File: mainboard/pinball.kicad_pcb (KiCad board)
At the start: 2 copper layers, 35 parts, among them CON1 AVR-ISP-6, IC1 ATMEGA328-A, P1 SCREW_PLACEHOLDER, P2 SCREW_PLACEHOLDER, P3 SCREW_PLACEHOLDER, P4 SCREW_PLACEHOLDER, P5 PWR, P6 SCORE_CONN, P7 CONN_02X24, Q1 Q_NMOS_GDS, Q2 Q_NPN_BEC, Q3 Q_NMOS_GDS, Q4 Q_NPN_BEC, Q5 Q_NMOS_GDS, Q6 Q_NPN_BEC, Q7 Q_NMOS_GDS, Q8 Q_NPN_BEC, U1 R-78B5.0-2.0, U2 Teensy3.2, Y1 Crystal

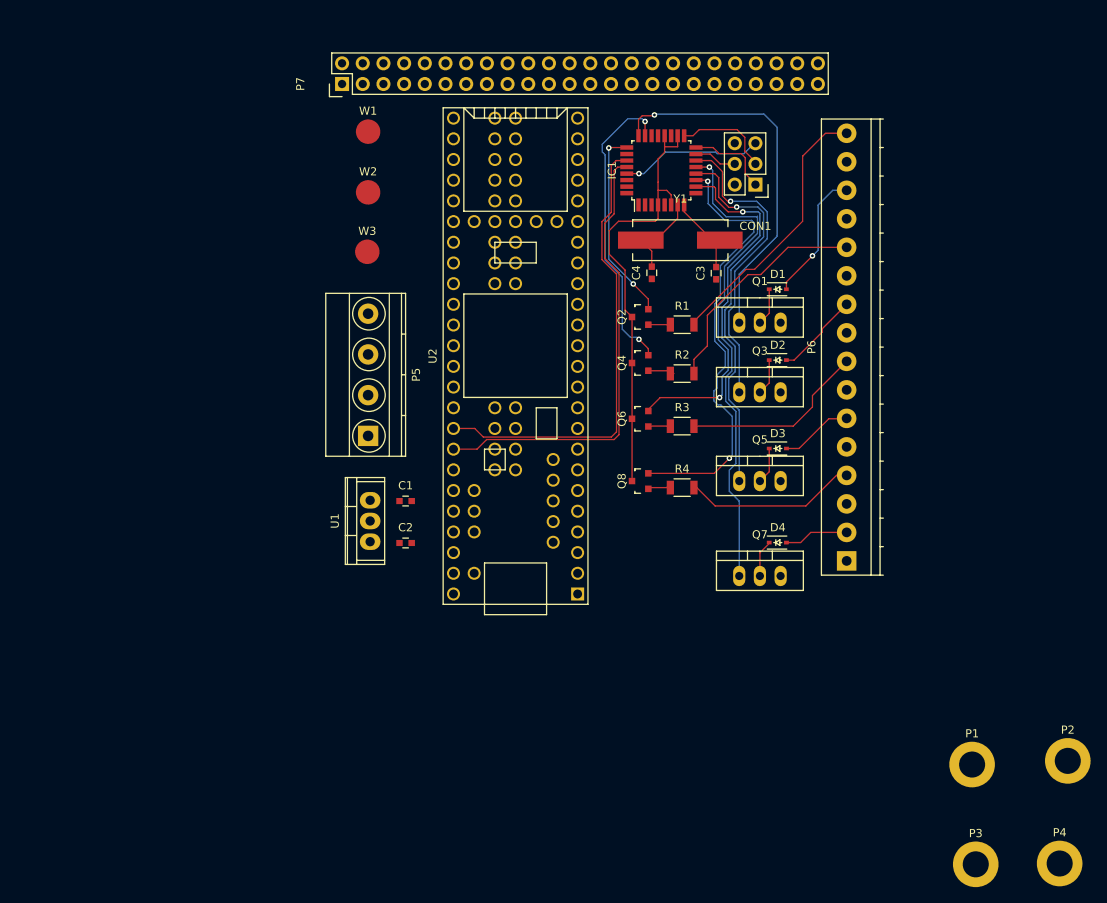
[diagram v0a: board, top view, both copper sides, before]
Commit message: KiCad 5.0 conversion. Start on slimming PCB.
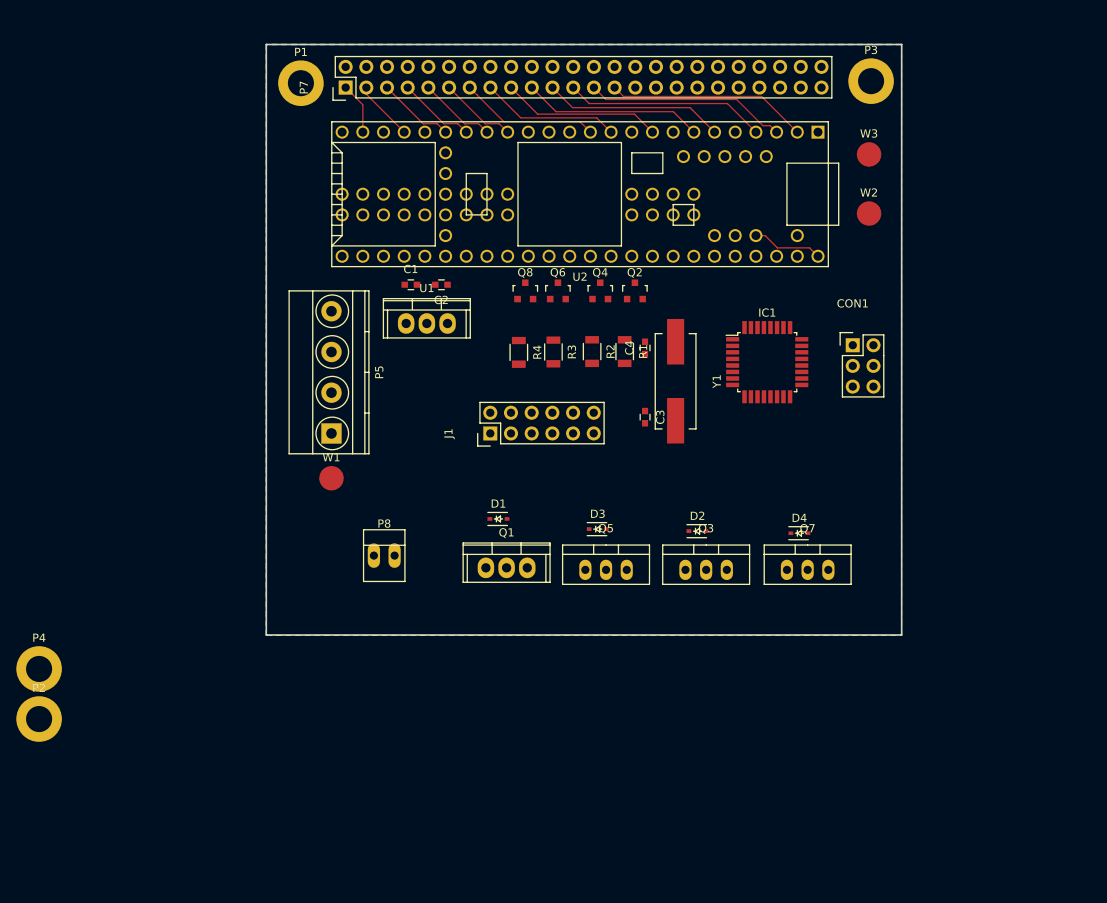
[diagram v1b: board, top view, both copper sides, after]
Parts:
- removed P6: SCORE_CONN, Terminal_Blocks:TerminalBlock_Pheonix_PT-3.5mm_16pol
- added J1: Conn_01x12, Pin_Headers:Pin_Header_Straight_2x06, F.Cu at (109.5, 87.8)
- added P8: Flipper Relay, Connect:PINHEAD1-2, F.Cu at (96.5, 102.8)
- Q1: footprint TO_SOT_Packages_THT:TO-220_Neutral123_Vertical -> Power_Integrations:TO-220
- moved P4 127.6 mm to (54.1, 116.7)
- moved P2 126.4 mm to (54.1, 122.8)
- moved P1 117.4 mm to (86.2, 44.8)
- moved P3 97.0 mm to (156.2, 44.5)
- moved W3 62.7 mm to (156.0, 53.5)
- moved W2 61.6 mm to (156.0, 60.8)
- moved D1 44.4 mm to (110.5, 98.2)
- moved Q1 43.3 mm to (111.5, 104.2)
- moved W1 42.8 mm to (90.0, 93.2)
- moved C2 32.0 mm to (103.5, 69.5), turned to 180 degrees
- moved Q8 27.3 mm to (113.8, 70.2), turned to 0 degrees
- moved IC1 26.9 mm to (143.5, 79.0), turned to 0 degrees
- moved C1 26.6 mm to (99.8, 69.5)
- moved R4 26.0 mm to (113.0, 77.8), turned to 270 degrees
- moved U1 25.2 mm to (101.7, 74.2), turned to 0 degrees
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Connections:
- C1 pad 1: Vin -> SCORE_OUT1B
- D1 pad 1: SCORE_OUT4 -> SCORE_OUT1B
- D1 pad 2: SCORE_OUT4 -> SCORE_OUT4A
- D2 pad 1: SCORE_OUT3 -> SCORE_OUT1B
- D2 pad 2: SCORE_OUT3 -> SCORE_OUT3A
- D3 pad 1: SCORE_OUT2 -> SCORE_OUT1B
- D3 pad 2: SCORE_OUT2 -> SCORE_OUT2A
- D4 pad 1: SCORE_OUT1 -> SCORE_OUT1B
- D4 pad 2: SCORE_OUT1 -> SCORE_OUT1A
- P1 pad 1: (no net) -> GND
- P2 pad 1: (no net) -> GND
- P3 pad 1: (no net) -> GND
- P4 pad 1: (no net) -> GND
- P5 pad 1: Vin -> SCORE_OUT1B
- P7 pad 1: SWITCH1 -> SWITCH16
- P7 pad 11: SWITCH6 -> SWITCH10
- P7 pad 13: SWITCH7 -> SWITCH8
- P7 pad 15: (no net) -> SWITCH7
- P7 pad 17: SWITCH9 -> SWITCH6
- P7 pad 19: SWITCH10 -> SWITCH5
- P7 pad 21: SWITCH11 -> SWITCH4
- P7 pad 23: SWITCH12 -> SWITCH3
- P7 pad 25: SWITCH13 -> SWITCH2
- P7 pad 27: SWITCH14 -> SWITCH1
- P7 pad 29: SWITCH15 -> SWITCH9
- P7 pad 3: SWITCH2 -> SWITCH15
- P7 pad 31: SWITCH16 -> SWITCH14
- P7 pad 5: SWITCH3 -> SWITCH13
- P7 pad 7: SWITCH4 -> SWITCH12
- P7 pad 9: SWITCH5 -> SWITCH11
- Q1 pad 2: SCORE_OUT4 -> SCORE_OUT4A
- Q3 pad 2: SCORE_OUT3 -> SCORE_OUT3A
- Q5 pad 2: SCORE_OUT2 -> SCORE_OUT2A
- Q7 pad 2: SCORE_OUT1 -> SCORE_OUT1A
- U1 pad 1: (no net) -> SCORE_OUT1B
- U1 pad 2: (no net) -> GND
- U1 pad 3: (no net) -> +5V
- U2 pad 12: (no net) -> SWITCH8
- U2 pad 24: CS3 -> (no net)
- U2 pad 31: SWITCH17 -> SWITCH14
- U2 pad 32: SWITCH18 -> SWITCH17
- U2 pad 33: SWITCH19 -> SWITCH18
- U2 pad 34: SWITCH20 -> SWITCH19
- U2 pad 35: SWITCH21 -> SWITCH20
- U2 pad 36: SWITCH22 -> SWITCH21
- U2 pad 37: (no net) -> FLIPPER_ON_RELAY
- U2 pad 41: SWITCH23 -> SWITCH22
- U2 pad 42: SWITCH24 -> SWITCH23
- U2 pad 43: SWITCH14 -> SWITCH24
- U2 pad 48: CS3 -> (no net)
- W1 pad 1: Vin -> SCORE_OUT1B
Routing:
- net SCORE1: track 58.6 -> 0.00 mm, vias 1 -> 0
- net SDA: track 56.8 -> 0.00 mm
- net SCL: track 56.4 -> 0.00 mm
- net SCORE_ZERO1: track 54.9 -> 0.00 mm, vias 2 -> 0
- net SCORE2: track 48.2 -> 0.00 mm, vias 1 -> 0
- net SCORE_ZERO2: track 47.2 -> 0.00 mm, vias 2 -> 0
- net +5V: track 55.3 -> 8.67 mm
- net SCORE4: track 45.9 -> 0.00 mm, vias 1 -> 0
- net SCORE3: track 37.8 -> 0.00 mm, vias 1 -> 0
- net SCORE_ZERO3: track 37.2 -> 0.00 mm, vias 2 -> 0
- net SCORE_ZERO_IN4: track 34.0 -> 0.00 mm
- net SCORE_ZERO_IN3: track 28.6 -> 0.00 mm
- net SWITCH3: track 0.00 -> 24.7 mm
- net SWITCH2: track 0.00 -> 24.7 mm
- net SWITCH1: track 0.00 -> 24.7 mm
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- added copper zone on B.Cu, net GND
- added copper zone on F.Cu, net GND
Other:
- board outline added: 78 x 72.5 mm

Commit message: Voltage dividers on switch pins
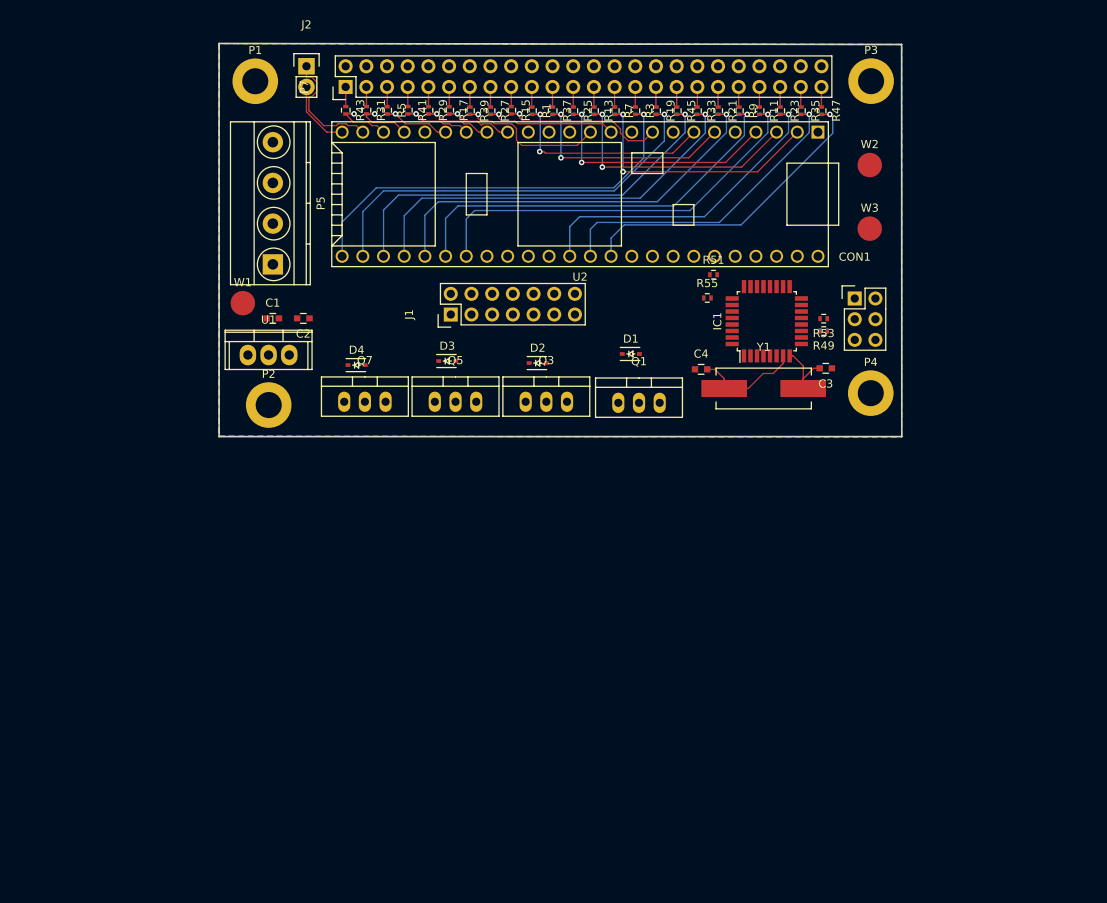
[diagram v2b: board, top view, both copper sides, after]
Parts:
- removed P8: Flipper Relay, Connect:PINHEAD1-2
- removed Q2, Q4, Q6, Q8: Q_NPN_BEC, TO_SOT_Packages_SMD:SOT-23
- added J2: Conn_01x02, Pin_Headers:Pin_Header_Straight_1x02, F.Cu at (86.9, 42.7)
- added R10: 620, Resistors_SMD:R_0402, B.Cu at (140.0, 48.1)
- added R11: 1.3k, Resistors_SMD:R_0402, F.Cu at (142.6, 48.1)
- added R12: 620, Resistors_SMD:R_0402, B.Cu at (142.6, 48.1)
- added R13: 1.3k, Resistors_SMD:R_0402, F.Cu at (122.2, 48.1)
- added R14: 620, Resistors_SMD:R_0402, B.Cu at (122.2, 48.1)
- added R15: 1.3k, Resistors_SMD:R_0402, F.Cu at (112.1, 48.1)
- added R16: 620, Resistors_SMD:R_0402, B.Cu at (112.1, 48.1)
- added R17: 1.3k, Resistors_SMD:R_0402, F.Cu at (104.5, 48.1)
- added R18: 620, Resistors_SMD:R_0402, B.Cu at (104.5, 48.1)
- added R19: 1.3k, Resistors_SMD:R_0402, F.Cu at (129.9, 48.1)
- added R20: 620, Resistors_SMD:R_0402, B.Cu at (129.9, 48.1)
- added R21: 1.3k, Resistors_SMD:R_0402, F.Cu at (137.5, 48.1)
- added R22: 620, Resistors_SMD:R_0402, B.Cu at (137.5, 48.1)
- added R23: 1.3k, Resistors_SMD:R_0402, F.Cu at (145.1, 48.1)
- added R24: 620, Resistors_SMD:R_0402, B.Cu at (145.1, 48.1)
- added R25: 1.3k, Resistors_SMD:R_0402, F.Cu at (119.7, 48.1)
- added R26: 620, Resistors_SMD:R_0402, B.Cu at (119.7, 48.1)
- added R27: 1.3k, Resistors_SMD:R_0402, F.Cu at (109.5, 48.1)
- added R28: 620, Resistors_SMD:R_0402, B.Cu at (109.5, 48.1)
- added R29: 1.3k, Resistors_SMD:R_0402, F.Cu at (101.9, 48.1)
- added R30: 620, Resistors_SMD:R_0402, B.Cu at (101.9, 48.1)
- added R31: 1.3k, Resistors_SMD:R_0402, F.Cu at (94.3, 48.1)
- added R32: 620, Resistors_SMD:R_0402, B.Cu at (94.3, 48.1)
- added R33: 1.3k, Resistors_SMD:R_0402, F.Cu at (134.9, 48.1)
- added R34: 620, Resistors_SMD:R_0402, B.Cu at (134.9, 48.1)
- added R35: 1.3k, Resistors_SMD:R_0402, F.Cu at (147.6, 48.1)
- added R36: 620, Resistors_SMD:R_0402, B.Cu at (147.6, 48.1)
- added R37: 1.3k, Resistors_SMD:R_0402, F.Cu at (117.2, 48.1)
- added R38: 620, Resistors_SMD:R_0402, B.Cu at (117.2, 48.1)
- added R39: 1.3k, Resistors_SMD:R_0402, F.Cu at (107.0, 48.1)
- added R40: 620, Resistors_SMD:R_0402, B.Cu at (107.0, 48.1)
- added R41: 1.3k, Resistors_SMD:R_0402, F.Cu at (99.4, 48.1)
- added R42: 620, Resistors_SMD:R_0402, B.Cu at (99.4, 48.1)
- added R43: 1.3k, Resistors_SMD:R_0402, F.Cu at (91.8, 48.1)
- added R44: 620, Resistors_SMD:R_0402, B.Cu at (91.8, 48.1)
- added R45: 1.3k, Resistors_SMD:R_0402, F.Cu at (132.4, 48.1)
- added R46: 620, Resistors_SMD:R_0402, B.Cu at (132.4, 48.1)
- added R47: 1.3k, Resistors_SMD:R_0402, F.Cu at (150.2, 48.1)
- added R48: 620, Resistors_SMD:R_0402, B.Cu at (150.2, 48.1)
- added R49: 1.3k, Resistors_SMD:R_0402, F.Cu at (150.4, 75.2)
- added R5: 1.3k, Resistors_SMD:R_0402, F.Cu at (96.8, 48.1)
- added R50: 620, Resistors_SMD:R_0402, B.Cu at (150.4, 75.2)
- added R51: 1.3k, Resistors_SMD:R_0402, F.Cu at (136.9, 68.3)
- added R52: 620, Resistors_SMD:R_0402, B.Cu at (136.9, 68.3)
- added R53: 1.3k, Resistors_SMD:R_0402, F.Cu at (150.4, 73.7)
- added R54: 620, Resistors_SMD:R_0402, B.Cu at (150.4, 73.7)
- added R55: 1.3k, Resistors_SMD:R_0402, F.Cu at (136.1, 71.1)
- added R56: 620, Resistors_SMD:R_0402, B.Cu at (136.1, 71.1)
- added R6: 620, Resistors_SMD:R_0402, B.Cu at (96.8, 48.1)
- added R7: 1.3k, Resistors_SMD:R_0402, F.Cu at (124.8, 48.1)
- added R8: 620, Resistors_SMD:R_0402, B.Cu at (124.8, 48.1)
- added R9: 1.3k, Resistors_SMD:R_0402, F.Cu at (140.0, 48.1)
- J1: value Conn_01x12 -> Conn_01x14; footprint Pin_Headers:Pin_Header_Straight_2x06 -> Pin_Headers:Pin_Header_Straight_2x07
- Q1: footprint Power_Integrations:TO-220 -> TO_SOT_Packages_THT:TO-220_Neutral123_Vertical
- R1, R3: value 1k -> 1.3k; footprint Resistors_SMD:R_1206 -> Resistors_SMD:R_0402
- R2, R4: value 1k -> 620; footprint Resistors_SMD:R_1206 -> Resistors_SMD:R_0402; moved to B.Cu
- U2: footprint teensy:Teensy35_36 -> teensy:Teensy35_36_edge
- moved P4 107.6 mm to (156.2, 82.8)
- moved Q7 58.1 mm to (94.1, 83.9)
- moved D4 58.1 mm to (93.1, 79.4)
- moved P2 47.8 mm to (82.3, 84.3)
- moved R4 32.9 mm to (127.3, 48.1), turned to 90 degrees
- moved R1 31.7 mm to (114.6, 48.1)
- moved R3 31.3 mm to (127.3, 48.1)
- moved R2 30.5 mm to (114.6, 48.1), turned to 90 degrees
- moved D2 28.5 mm to (115.3, 79.1)
- moved Q3 28.5 mm to (116.4, 83.9)
- moved D3 27.7 mm to (104.2, 78.9)
- moved Q5 27.7 mm to (105.2, 83.9)
- moved D1 26.0 mm to (126.8, 78.0)
- moved Q1 26.0 mm to (127.8, 84.0)
- moved W1 24.1 mm to (79.1, 71.8)
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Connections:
- net SCORE_OUT1B renamed Vin
- J1 pad 10: SCORE_ZERO_IN2 -> SCORE_ZERO_IN4
- J1 pad 12: SCORE_ZERO_IN4 -> SCORE_ZERO_IN2
- J1 pad 9: SCORE_ZERO_IN1 -> FLIPPER_ON_RELAY
- R1 pad 1: Net-(Q2-Pad1) -> SWITCH5
- R1 pad 2: SCORE_ZERO_IN4 -> SWITCH_LOW5
- R2 pad 1: Net-(Q4-Pad1) -> SWITCH_LOW5
- R2 pad 2: SCORE_ZERO_IN3 -> GND
- R3 pad 1: Net-(Q6-Pad1) -> SWITCH9
- R3 pad 2: SCORE_ZERO_IN2 -> SWITCH_LOW9
- R4 pad 1: Net-(Q8-Pad1) -> SWITCH_LOW9
- R4 pad 2: SCORE_ZERO_IN1 -> GND
- U2 pad 11: SWITCH7 -> SWITCH_LOW7
- U2 pad 12: SWITCH8 -> SWITCH_LOW8
- U2 pad 16: SWITCH10 -> SWITCH_LOW10
- U2 pad 17: SWITCH11 -> SWITCH_LOW11
- U2 pad 18: SWITCH12 -> SWITCH_LOW12
- U2 pad 19: SWITCH13 -> SWITCH_LOW13
- U2 pad 2: SWITCH1 -> SWITCH_LOW1
- U2 pad 21: SWITCH15 -> SWITCH_LOW15
- U2 pad 22: (no net) -> SWITCH_LOW16
- U2 pad 23: SWITCH16 -> RX
- U2 pad 24: (no net) -> TX
- U2 pad 3: SWITCH2 -> SWITCH_LOW2
- U2 pad 30: SWITCH9 -> SWITCH_LOW9
- U2 pad 31: SWITCH14 -> SWITCH_LOW14
- U2 pad 32: SWITCH17 -> SWITCH_LOW17
- U2 pad 33: SWITCH18 -> SWITCH_LOW18
- U2 pad 34: SWITCH19 -> SWITCH_LOW19
- U2 pad 35: SWITCH20 -> SWITCH_LOW20
- U2 pad 36: SWITCH21 -> SWITCH_LOW21
- U2 pad 4: SWITCH3 -> SWITCH_LOW3
- U2 pad 41: SWITCH22 -> SWITCH_LOW22
- U2 pad 42: SWITCH23 -> SWITCH_LOW23
- U2 pad 43: SWITCH24 -> SWITCH_LOW24
- U2 pad 6: SWITCH4 -> SWITCH_LOW4
- U2 pad 7: SWITCH5 -> SWITCH_LOW5
- U2 pad 9: SWITCH6 -> SWITCH_LOW6
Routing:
- net SWITCH_LOW9: track 0.00 -> 51.9 mm, vias 0 -> 1
- net SWITCH_LOW14: track 0.00 -> 51.4 mm, vias 0 -> 1
- net SWITCH_LOW17: track 0.00 -> 50.9 mm, vias 0 -> 1
- net SWITCH_LOW19: track 0.00 -> 50.5 mm, vias 0 -> 1
- net SWITCH_LOW18: track 0.00 -> 50.5 mm, vias 0 -> 1
- net SWITCH_LOW20: track 0.00 -> 50.3 mm, vias 0 -> 1
- net SWITCH_LOW21: track 0.00 -> 50.3 mm, vias 0 -> 1
- net SWITCH_LOW22: track 0.00 -> 39.6 mm, vias 0 -> 1
- net SWITCH_LOW23: track 0.00 -> 39.4 mm, vias 0 -> 1
- net SWITCH_LOW24: track 0.00 -> 39.3 mm, vias 0 -> 1
- net SWITCH_LOW1: track 0.00 -> 32.5 mm, vias 0 -> 2
- net SWITCH_LOW2: track 0.00 -> 31.7 mm, vias 0 -> 2
- net SWITCH_LOW3: track 0.00 -> 30.9 mm, vias 0 -> 2
- net SWITCH_LOW4: track 0.00 -> 27.5 mm, vias 0 -> 2
- net SWITCH_LOW5: track 0.00 -> 26.7 mm, vias 0 -> 2
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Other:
- board size 78 x 72.5 mm -> 83.8 x 48.3 mm

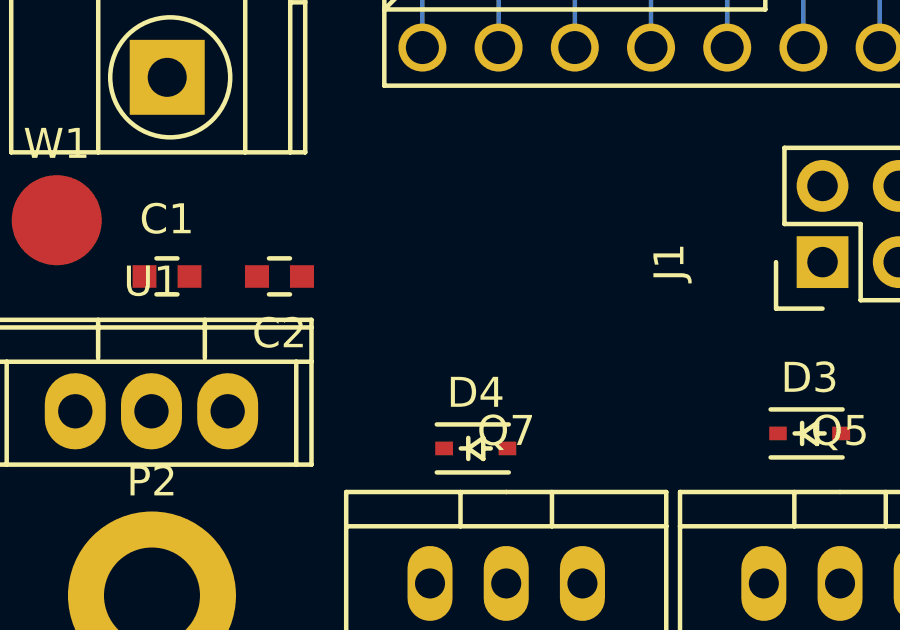
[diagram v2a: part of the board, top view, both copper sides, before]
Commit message: Add power LED
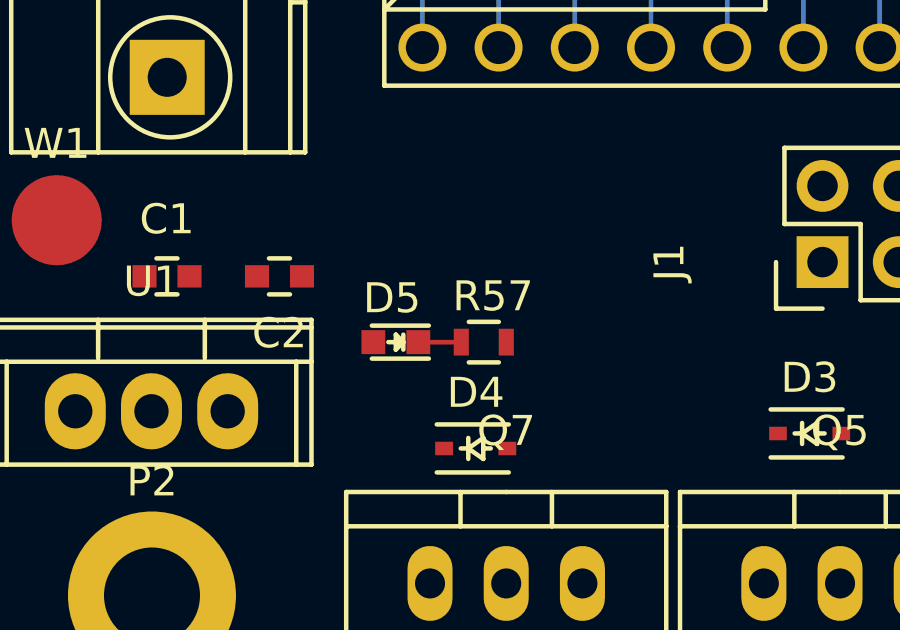
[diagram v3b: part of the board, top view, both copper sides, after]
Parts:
- added D5: LED, LEDs:LED-0603, F.Cu at (90.4, 75.8)
- added R57: 150, Resistors_SMD:R_0603, F.Cu at (93.4, 75.8)
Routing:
- net Net-(D5-Pad1): track 0.00 -> 1.43 mm
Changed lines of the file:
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@@
     (thickness 1.6)
     (drawings 4)
-    (tracks 332)
+    (tracks 333)
     (zones 0)
-    (modules 84)
-    (nets 79)
+    (modules 86)
+    (nets 80)
   )
   (page A4)
@@
   (net 77 SWITCH_LOW17)
   (net 78 SWITCH_LOW24)
+  (net 79 "Net-(D5-Pad1)")
   (net_class Default "This is the default net class."
     (clearance 0.1524)
@@
     (add_net MISO_AVR)
     (add_net MOSI_AVR)
+    (add_net "Net-(D5-Pad1)")
     (add_net RST)
     (add_net RX)
@@
     )
   )
+  (module LEDs:LED-0603 (layer F.Cu)
+    (at 90.424 75.819 180)
+    (descr "LED 0603 smd package")
+    (tags "LED led 0603 SMD smd SMT smt smdled SMDLED smtled SMTLED")
+    (attr smd)
+    (fp_text reference D5 (at 0.127 1.4605 180) (layer F.SilkS)
+      (effects (font (size 1 1) (thickness 0.15)))
+    )
+    (fp_text value LED (at 0 1.5 180) (layer F.Fab)
+      (effects (font (size 1 1) (thickness 0.15)))
+    )
+    (fp_line (start -1.1 0.55) (end 0.8 0.55) (layer F.SilkS) (width 0.15))
+    (fp_line (start -1.1 -0.55) (end 0.8 -0.55) (layer F.SilkS) (width 0.15))
+    (fp_line (start -0.2 0) (end 0.25 0) (layer F.SilkS) (width 0.15))
+    (fp_line (start -0.25 -0.25) (end -0.25 0.25) (layer F.SilkS) (width 0.15))
+    (fp_line (start -0.25 0) (end 0 -0.25) (layer F.SilkS) (width 0.15))
+    (fp_line (start 0 -0.25) (end 0 0.25) (layer F.SilkS) (width 0.15))
+    (fp_line (start 0 0.25) (end -0.25 0) (layer F.SilkS) (width 0.15))
+    (fp_line (start 1.4 -0.75) (end 1.4 0.75) (layer F.CrtYd) (width 0.05))
+    (fp_line (start 1.4 0.75) (end -1.4 0.75) (layer F.CrtYd) (width 0.05))
+    (fp_line (start -1.4 0.75) (end -1.4 -0.75) (layer F.CrtYd) (width 0.05))
+    (fp_line (start -1.4 -0.75) (end 1.4 -0.75) (layer F.CrtYd) (width 0.05))
+    (pad 2 smd rect (at 0.7493 0) (size 0.79756 0.79756) (layers F.Cu F.Paste F.Mask)
+      (net 2 +5V))
+    (pad 1 smd rect (at -0.7493 0) (size 0.79756 0.79756) (layers F.Cu F.Paste F.Mask)
+      (net 79 "Net-(D5-Pad1)"))
+  )
+  (module Resistors_SMD:R_0603 (layer F.Cu)
+    (at 93.357 75.819)
+    (descr "Resistor SMD 0603, reflow soldering, Vishay (see dcrcw.pdf)")
+    (tags "resistor 0603")
+    (attr smd)
+    (fp_text reference R57 (at 0.3055 -1.524) (layer F.SilkS)
+      (effects (font (size 1 1) (thickness 0.15)))
+    )
+    (fp_text value 150 (at 0 1.9) (layer F.Fab)
+      (effects (font (size 1 1) (thickness 0.15)))
+    )
+    (fp_line (start -1.3 -0.8) (end 1.3 -0.8) (layer F.CrtYd) (width 0.05))
+    (fp_line (start -1.3 0.8) (end 1.3 0.8) (layer F.CrtYd) (width 0.05))
+    (fp_line (start -1.3 -0.8) (end -1.3 0.8) (layer F.CrtYd) (width 0.05))
+    (fp_line (start 1.3 -0.8) (end 1.3 0.8) (layer F.CrtYd) (width 0.05))
+    (fp_line (start 0.5 0.675) (end -0.5 0.675) (layer F.SilkS) (width 0.15))
+    (fp_line (start -0.5 -0.675) (end 0.5 -0.675) (layer F.SilkS) (width 0.15))
+    (pad 1 smd rect (at -0.75 0) (size 0.5 0.9) (layers F.Cu F.Paste F.Mask)
+      (net 79 "Net-(D5-Pad1)"))
+    (pad 2 smd rect (at 0.75 0) (size 0.5 0.9) (layers F.Cu F.Paste F.Mask)
+      (net 1 GND))
+    (model Resistors_SMD.3dshapes/R_0603.wrl
+      (at (xyz 0 0 0))
+      (scale (xyz 1 1 1))
+      (rotate (xyz 0 0 0))
+    )
+  )
   (gr_line (start 160 40) (end 76.2 39.878) (layer Edge.Cuts) (width 0.2))
   (gr_line (start 160.02 88.138) (end 160 40) (layer Edge.Cuts) (width 0.2))
@@
   (segment (start 151.1935 48.5775) (end 151.536399 48.920399) (width 0.1524) (layer B.Cu) (net 78))
   (segment (start 151.536399 48.920399) (end 151.536399 50.901601) (width 0.1524) (layer B.Cu) (net 78))
+  (segment (start 91.1733 75.819) (end 92.607 75.819) (width 0.1524) (layer F.Cu) (net 79))
   (zone (net 1) (net_name GND) (layer F.Cu) (hatch edge 0.508)
     (connect_pads (clearance 0.508))
